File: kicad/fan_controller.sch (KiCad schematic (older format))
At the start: 43 parts, among them P1 CONN_01X04, P2 CONN_01X05, P3 CONN_01X04, P4 CONN_01X04, P5 CONN_01X04, P6 CONN_01X04, Q1 Q_NPN_BEC, Q2 Q_NPN_BEC, Q3 Q_NPN_BEC, Q4 Q_NPN_BEC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

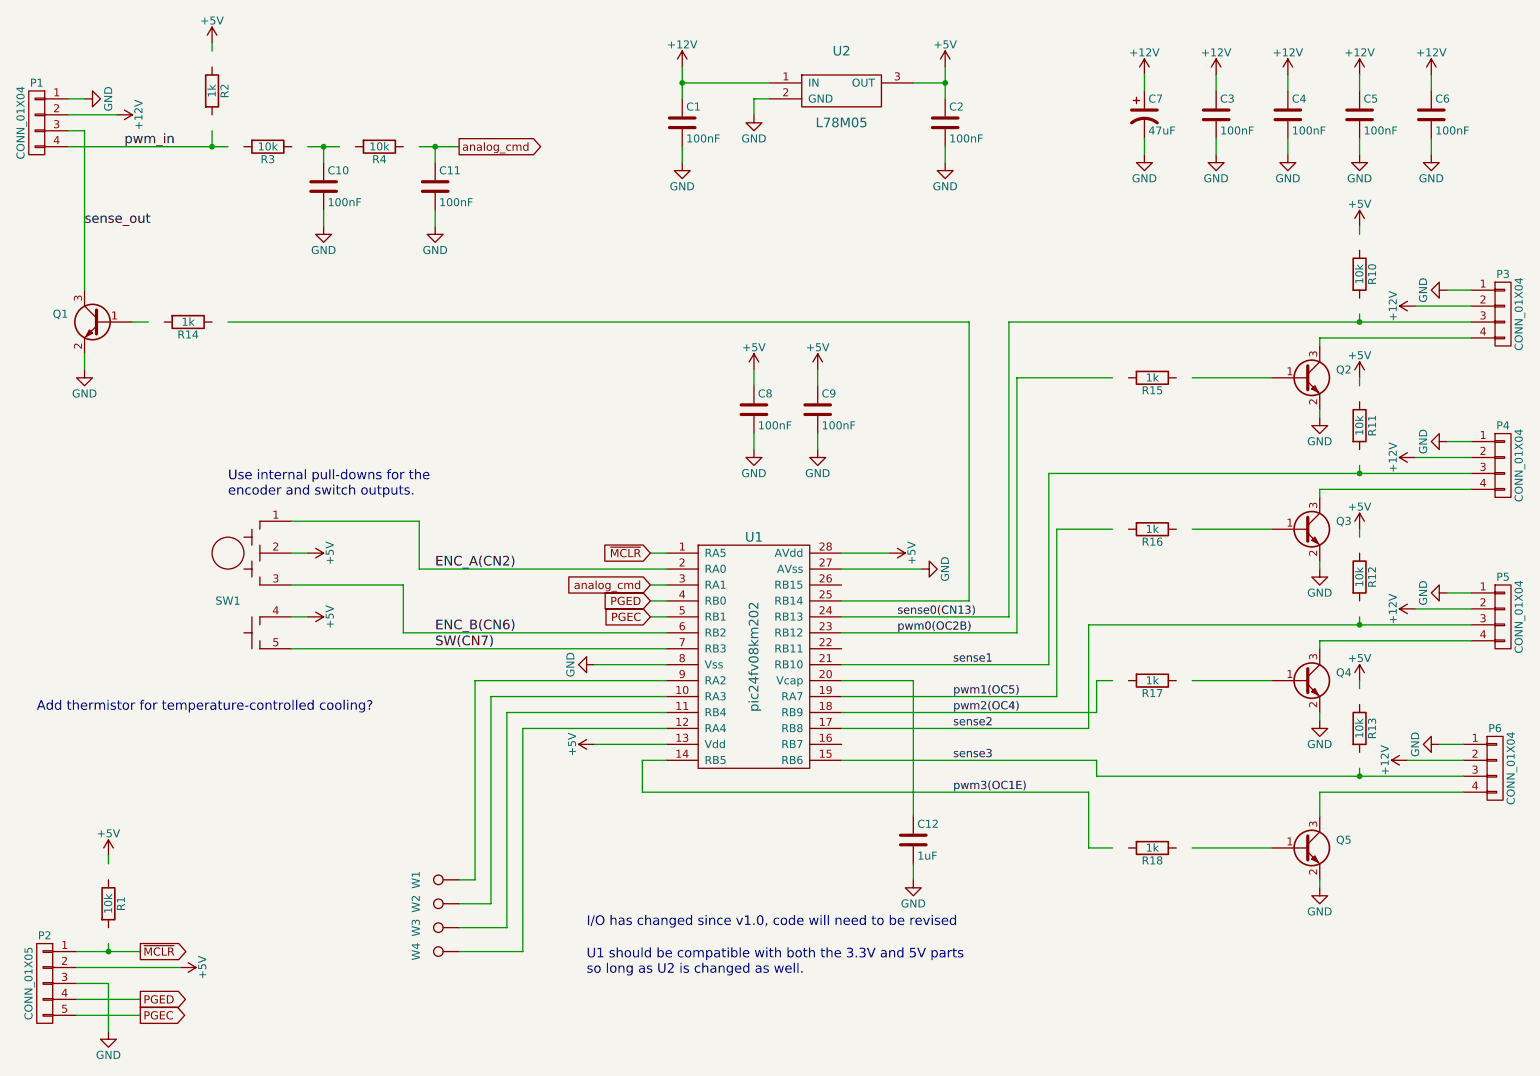
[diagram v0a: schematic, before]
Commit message: Added LEDs, fixed #2
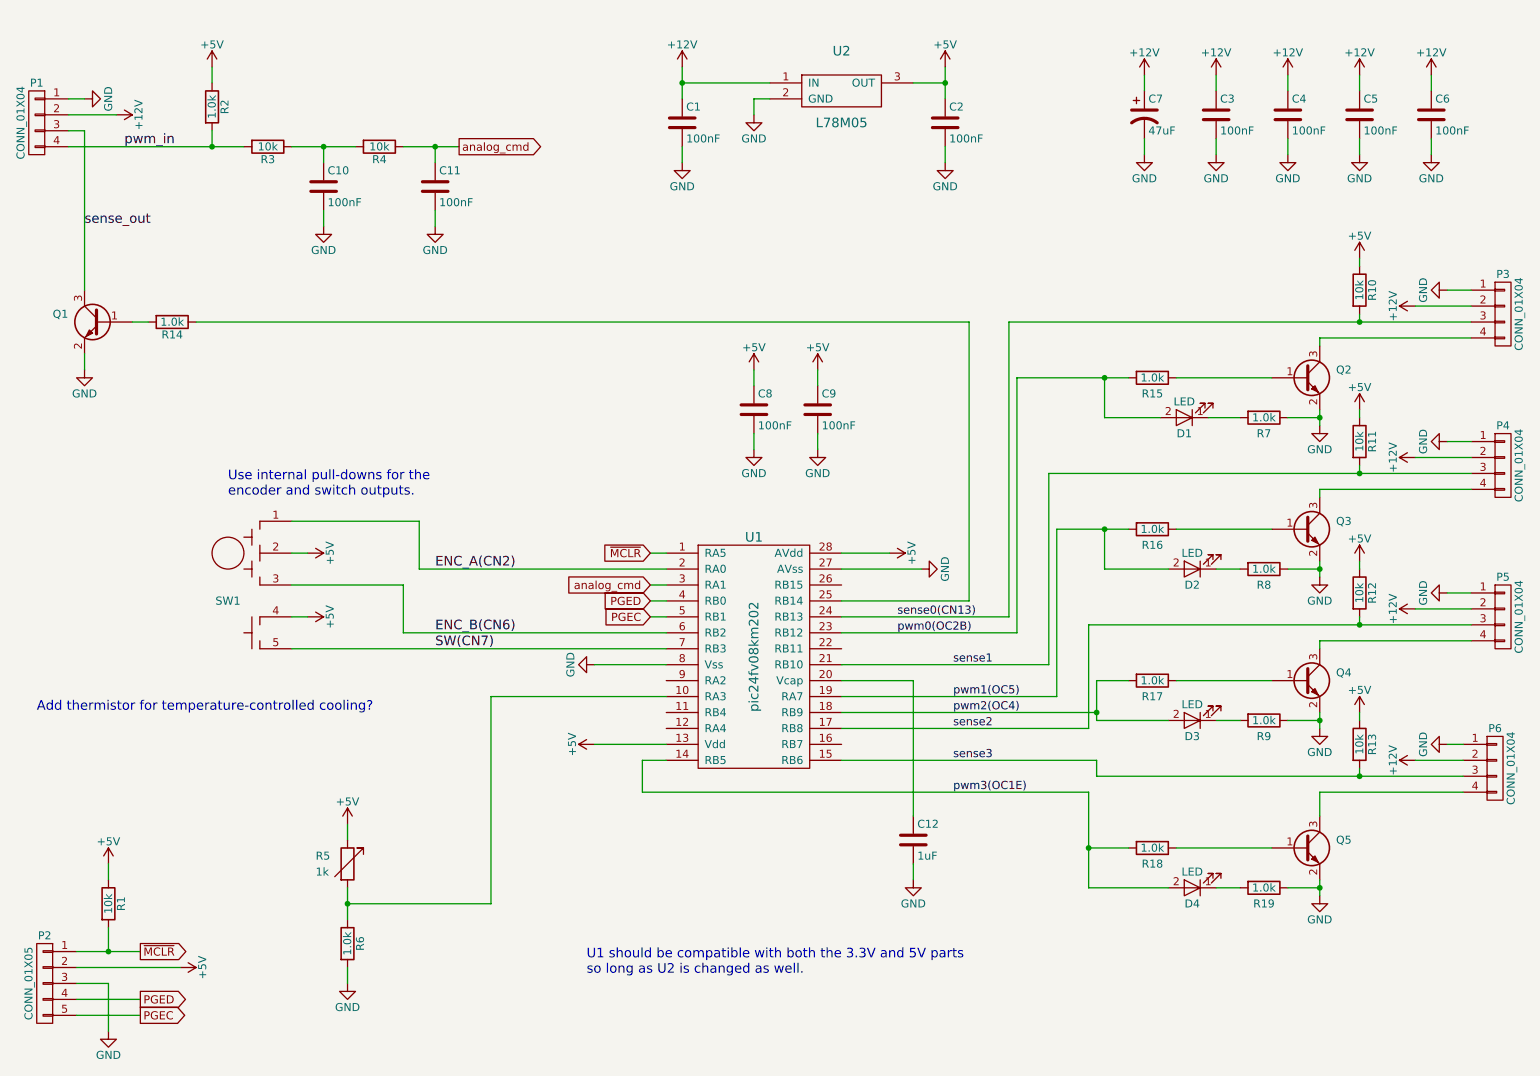
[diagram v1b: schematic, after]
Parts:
- removed W1, W2, W3, W4: TEST_1P, Connect:PINTST, symbol TEST_1P
- added D1, D2, D3, D4: LED, Diodes_SMD:D_0805, symbol LED
- added R19, R6, R7, R8, R9: 1.0k, Resistors_SMD:R_0603, symbol R
- added R5: 1k, Diodes_SMD:D_0805, symbol R_Variable
- R1, R10, R11, R12, R13, R3, R4: footprint kicad_pcb:SM_0603 -> Resistors_SMD:R_0603
- R14, R15, R16, R17, R18, R2: value 1k -> 1.0k; footprint kicad_pcb:SM_0603 -> Resistors_SMD:R_0603
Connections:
- wire segments 138 -> 146
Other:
- note removed: "I/O has changed since v1.0, code will need to be revised"

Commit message: Updating to v1.2 (adding thermistor and LED)
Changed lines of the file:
@@
 LIBS:contrib
 LIBS:valves
+LIBS:schematic
 LIBS:fan_controller-cache
 EELAYER 25 0
@@
 Sheet 1 1
 Title "fan controller"
-Date "2016-07-21"
-Rev "1.1"
+Date "2017-06-07"
+Rev "1.2"
 Comp "for(embed)"
 Comment1 "www.forembed.com"
@@
 	1    0    0    -1
 $EndComp
+$Comp
+L LOGO #G?
+U 1 1 5938AD3B
+P 7200 6750
+F 0 "#G?" H 7200 6595 60  0001 C CNN
+F 1 "LOGO" H 7200 6905 60  0001 C CNN
+F 2 "" H 7200 6750 60  0001 C CNN
+F 3 "" H 7200 6750 60  0001 C CNN
+	1    7200 6750
+	1    0    0    -1
+$EndComp
